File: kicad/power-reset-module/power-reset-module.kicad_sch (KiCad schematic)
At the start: 11 parts, among them U1 74LS14, U2 74LS32, U3 74LS245

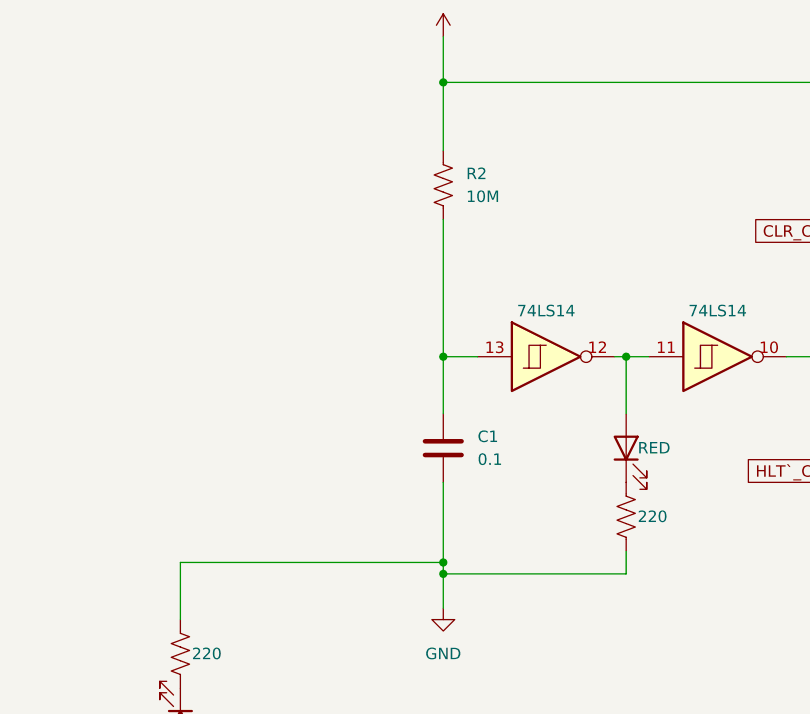
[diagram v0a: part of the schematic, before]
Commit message: Add a reset button to the Power-Up Module
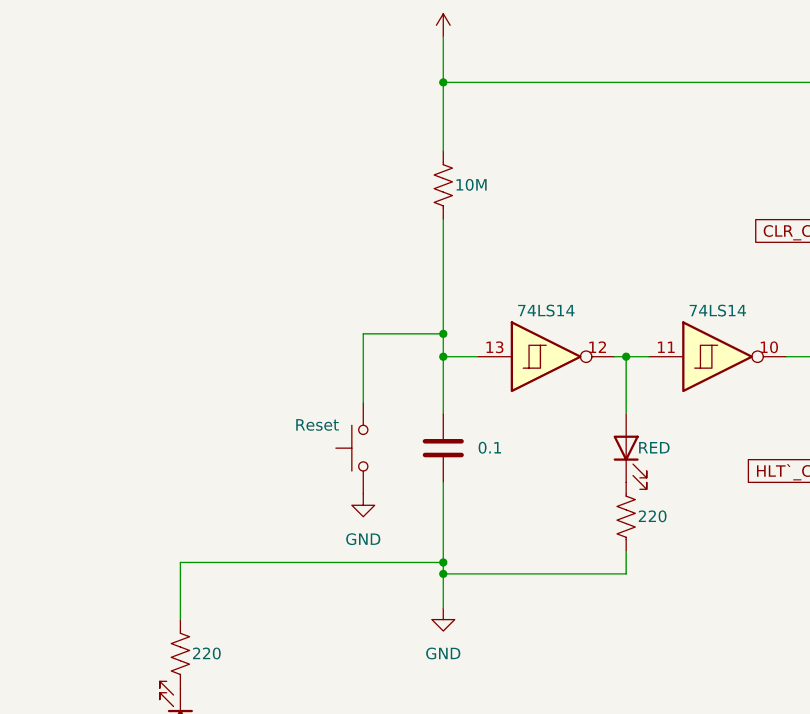
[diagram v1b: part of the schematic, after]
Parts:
- added SW?: Reset, symbol Switch:SW_Push
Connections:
- net GND: now also SW?.1
- net at C1.1, R2.2, U1.13: now also SW?.2
